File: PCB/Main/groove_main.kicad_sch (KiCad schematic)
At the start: 38 parts, among them J1 Left_X, J2 Left_Y, J3 Right_X, J4 Right_Y, J5 Left_X, J6 Left_Y, J7 Right_X, J8 Right_Y, U2 Pico, U3 CD4052B

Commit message: Main PCB progress 50%
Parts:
- removed D20, D21, D22, D23, D24: WS2812B_Unified, groove_pico:WS2812B-2835, symbol groove_pico:WS2812B_Unified
- added C1, C2, C3, C4, C5, C6, C7, C8, C9: 0.1uF, Capacitor_SMD:C_0603_1608Metric_Pad1.08x0.95mm_HandSolder, symbol Device:C
- added J10: Left_Y, groove_pico:Solder_3P_S, symbol Connector_Generic:Conn_01x03
- added J11: Right_X, groove_pico:Solder_3P_S, symbol Connector_Generic:Conn_01x03
- added J12: Right_Y, groove_pico:Solder_3P_S, symbol Connector_Generic:Conn_01x03
- added J9: Left_X, groove_pico:Solder_3P_S, symbol Connector_Generic:Conn_01x03
- added SW1, SW2, SW3: SWITCH_SPST, groove_pico:EVQP1K05M, symbol agg:SWITCH_SPST
- added U3: LM4040DBZ-3, Package_TO_SOT_SMD:SOT-23, symbol Reference_Voltage:LM4040DBZ-3
- J1, J2, J3, J4: footprint Connector_PinHeader_1.27mm:PinHeader_1x03_P1.27mm_Vertical -> groove_pico:SH1.25_Thruhole_3P
- J5, J6, J7, J8: footprint Connector_JST:JST_GH_BM03B-GHS-TBT_1x03-1MP_P1.25mm_Vertical -> groove_pico:SH1.25mm_3P_SMD
- renumbered U2 to U1, U3 to U2
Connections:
- net +3.3VADC: now also J1.3 (Pin_3), J2.3 (Pin_3), J3.3 (Pin_3), J4.3 (Pin_3), J5.3 (Pin_3), J6.3 (Pin_3), J7.3 (Pin_3), J8.3 (Pin_3), C9.1, J10.3 (Pin_3), J11.3 (Pin_3), J12.3 (Pin_3), J9.3 (Pin_3), U3.1 (K); no longer J1.1 (Pin_1), J2.1 (Pin_1), J3.1 (Pin_1), J4.1 (Pin_1), J5.1 (Pin_1), J6.1 (Pin_1), J7.1 (Pin_1), J8.1 (Pin_1)
- net +3V3: now also C3.1
- net +5V: now also C1.1, C2.1, C4.1, C5.1, C6.1, C7.1, C8.1
- net GND: now also C1.2, C2.2, C3.2, C4.2, C5.2, C6.2, C7.2, C8.2; no longer J1.3 (Pin_3), J2.3 (Pin_3), J3.3 (Pin_3), J4.3 (Pin_3), J5.3 (Pin_3), J6.3 (Pin_3), J7.3 (Pin_3), J8.3 (Pin_3)
- net LX: now also J9.2 (Pin_2)
- net LY: now also J10.2 (Pin_2)
- net RX: now also J11.2 (Pin_2)
- net RY: now also J12.2 (Pin_2)
- net GNDREF: now reaches U1.34 (GPIO28_ADC2)
- net GNDREF: now also J1.1 (Pin_1), J2.1 (Pin_1), J3.1 (Pin_1), J4.1 (Pin_1), J5.1 (Pin_1), J6.1 (Pin_1), J7.1 (Pin_1), J8.1 (Pin_1), C9.2, J10.1 (Pin_1), J11.1 (Pin_1), J12.1 (Pin_1), J9.1 (Pin_1), U3.2 (A)
- no-connect marks 33 -> 32

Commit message: Main PCB progress 70%
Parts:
- added D20, D21, D22, D23, D24, D25, D26, D27, D32, D33, D34, D35, D36, D37, D38, D39: WS2812B_Unified, groove_pico:WS2812B-4020, symbol groove_pico:WS2812B_Unified
- added D28, D29, D30, D31, D40, D41, D42, D43: WS2812B_Unified, groove_pico:WS2812B-4020_UP, symbol groove_pico:WS2812B_Unified
- added J13, J14: SW, groove_pico:Solder_1P, symbol Connector:TestPoint
- added J15, J19: V, groove_pico:Solder_1P, symbol Connector:TestPoint
- added J16, J20: LED, groove_pico:Solder_1P, symbol Connector:TestPoint
- added J18, J22: G, groove_pico:Solder_1P, symbol Connector:TestPoint
- added R4, R5: 10, Resistor_SMD:R_0603_1608Metric, symbol Device:R_Small
- added SCR1, SCR2, SCR3, SCR4, SCR5, SCR6, SCR7, SCR8: ScrewHole, groove_pico:Hole2.0, symbol groove_pico:ScrewHole
- added SW4, SW5: SWITCH_SPST, groove_pico:SW_Kailh_Choc_V1V2_1.00u_LED, symbol agg:SWITCH_SPST
- renumbered R2 to R1, R3 to R2, R1 to R3
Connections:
- net +5V: now also D20.V (VDD), D21.V (VDD), D22.V (VDD), D23.V (VDD), D24.V (VDD), D25.V (VDD), D26.V (VDD), D27.V (VDD), D28.V (VDD), D29.V (VDD), D30.V (VDD), D31.V (VDD), D32.V (VDD), D33.V (VDD), D34.V (VDD), D35.V (VDD), D36.V (VDD), D37.V (VDD), D38.V (VDD), D39.V (VDD), D40.V (VDD), D41.V (VDD), D42.V (VDD), D43.V (VDD), J15.1, J19.1
- net GND: now also SW1.2 ("~{"}), SW2.2 ("~{"}), SW3.2 ("~{"}), U1.13 (GND), U1.23 (GND), D20.G (VSS), D21.G (VSS), D22.G (VSS), D23.G (VSS), D24.G (VSS), D25.G (VSS), D26.G (VSS), D27.G (VSS), D28.G (VSS), D29.G (VSS), D30.G (VSS), D31.G (VSS), D32.G (VSS), D33.G (VSS), D34.G (VSS), D35.G (VSS), D36.G (VSS), D37.G (VSS), D38.G (VSS), D39.G (VSS), D40.G (VSS), D41.G (VSS), D42.G (VSS), D43.G (VSS), J18.1, J22.1, SW4.2 ("~{"}), SW5.2 ("~{"})
- net GNDREF: now also U1.33 (AGND); no longer U1.34 (GPIO28_ADC2)
- net RGB: now also U1.17 (GPIO13); no longer U1.16 (GPIO12)
- net at SW1.1 ("~{"}): now also U1.1 (GPIO0)
- net at U1.15 (GPIO11): now also R5.2
- net at U1.2 (GPIO1): now also SW2.1 ("~{"})
- net at U1.4 (GPIO2): now also SW3.1 ("~{"})
- new net: D20.I (In), J16.1, R4.1
- new net: D27.O (Out), D28.I (In)
- new net: D28.O (Out), D29.I (In)
- new net: D32.I (In), J20.1, R5.1
- new net: J13.1, SW4.1 ("~{"})
- new net: D35.O (Out), D36.I (In)
- new net: D36.O (Out), D37.I (In)
- new net: D29.O (Out), D30.I (In)
- new net: D30.O (Out), D31.I (In)
- new net: D41.O (Out), D42.I (In)
- new net: D42.O (Out), D43.I (In)
- new net: D34.O (Out), D35.I (In)
- new net: D20.O (Out), D21.I (In)
- new net: D21.O (Out), D22.I (In)
- new net: D22.O (Out), D23.I (In)
- new net: D23.O (Out), D24.I (In)
- new net: D26.O (Out), D27.I (In)
- new net: D33.O (Out), D34.I (In)
- new net: D37.O (Out), D38.I (In)
- new net: R4.2, U1.16 (GPIO12)
- new net: D38.O (Out), D39.I (In)
- new net: D39.O (Out), D40.I (In)
- new net: D25.O (Out), D26.I (In)
- new net: D40.O (Out), D41.I (In)
- new net: D32.O (Out), D33.I (In)
- new net: D24.O (Out), D25.I (In)
- new net: J14.1, SW5.1 ("~{"})
- no-connect marks 32 -> 26
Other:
- moved on the sheet: C1, C2, C3, C4, C5, C6, C7, C8, C9, R3

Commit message: Main PCB progress 85%
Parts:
- added J17, J21: LED, groove_pico:Solder_1P_S, symbol Connector:TestPoint
- added J23, J24: SW, groove_pico:Solder_1P_S, symbol Connector:TestPoint
- added J25, J26: V, groove_pico:Solder_1P_S, symbol Connector:TestPoint
- added J27, J28: G, groove_pico:Solder_1P_S, symbol Connector:TestPoint
- J13, J14, J15, J16, J18, J19, J20, J22: footprint groove_pico:Solder_1P -> groove_pico:Solder_1P_S
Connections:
- net +5V: now also J25.1, J26.1
- net GND: now also SW4.1 ("~{"}), SW5.1 ("~{"}), U1.8 (GND), U2.6 (INH), J27.1, J28.1; no longer SW4.2 ("~{"}), SW5.2 ("~{"}), U1.13 (GND)
- net at D20.I (In), J16.1: no longer R4.1
- net at D32.I (In), J20.1: no longer R5.1
- net at J13.1: now also SW4.2 ("~{"}); no longer SW4.1 ("~{"})
- net at U1.1 (GPIO0): now also SW3.1 ("~{"}); no longer SW1.1 ("~{"})
- net at U1.11 (GPIO8): now also J23.1
- net at U1.12 (GPIO9): now also J24.1
- net at U1.4 (GPIO2): now also SW1.1 ("~{"}); no longer SW3.1 ("~{"})
- net at U1.40 (VBUS): now also USB1.11 (VBUS), USB1.2 (VBUS)
- net at J14.1: now also SW5.2 ("~{"}); no longer SW5.1 ("~{"})
- net RGB: no longer names the net of R3.2, U1.17 (GPIO13)
- new net: J17.1, R4.1
- new net: J21.1, R5.1
- no-connect marks 26 -> 24
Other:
- moved on the sheet: J16, J20, R3, SW2

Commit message: Main PCB v1.0
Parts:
- added SCR10, SCR11, SCR12, SCR13, SCR14, SCR15, SCR16, SCR9: ScrewHole, groove_pico:Hole2.0, symbol groove_pico:ScrewHole
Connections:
- net GND: now also U1.28 (GND)
- net at J17.1, R4.1: now also D20.I (In), J16.1
- net at D32.I (In), J20.1: now also J21.1, R5.1
- net SW_L: now reaches J13.1, SW4.2 ("~{"})
- net SW_L: now also J24.1, U1.12 (GPIO9)
- net SW_R: now reaches J23.1, U1.11 (GPIO8)
- net SW_R: now also J14.1, SW5.2 ("~{"})
- no-connect marks 24 -> 25
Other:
- moved on the sheet: J21, R5

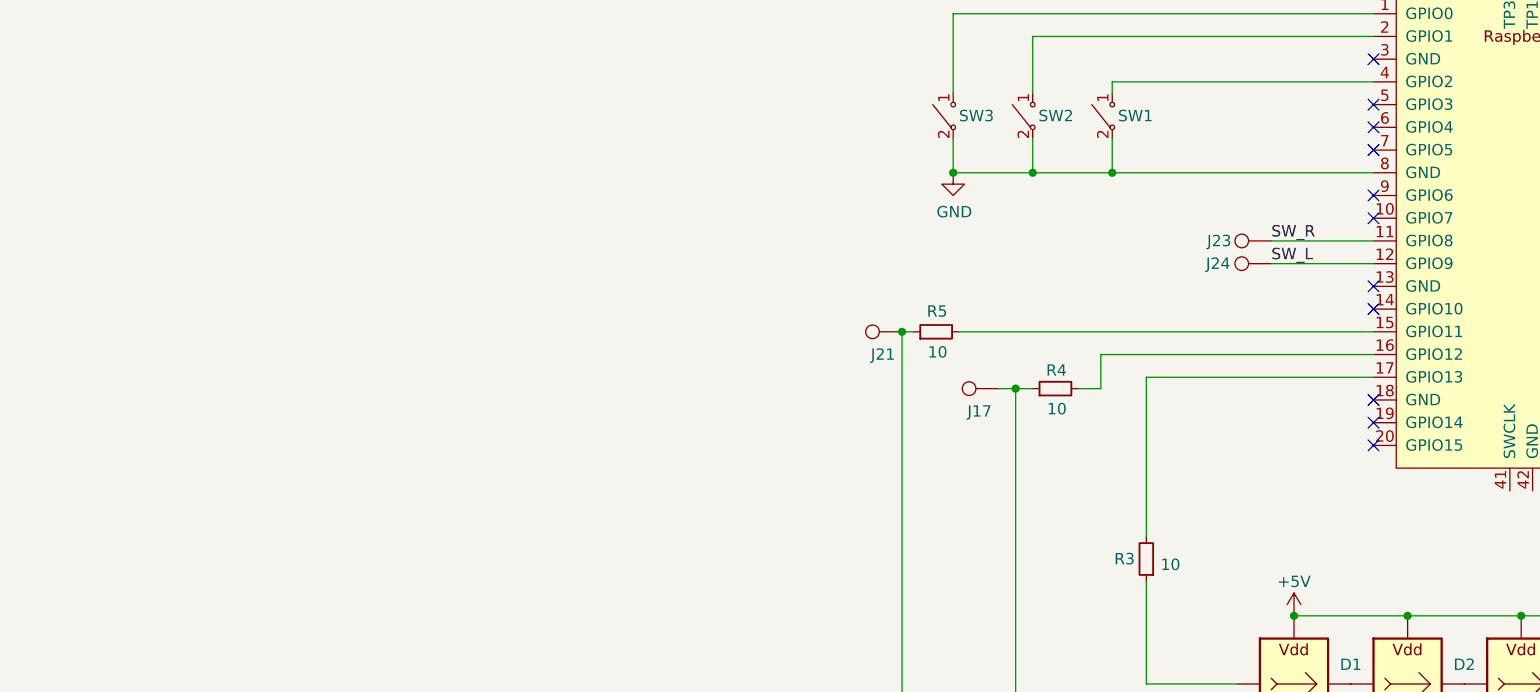
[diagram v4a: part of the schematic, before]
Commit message: Add slots in PCB for Hall gimbals
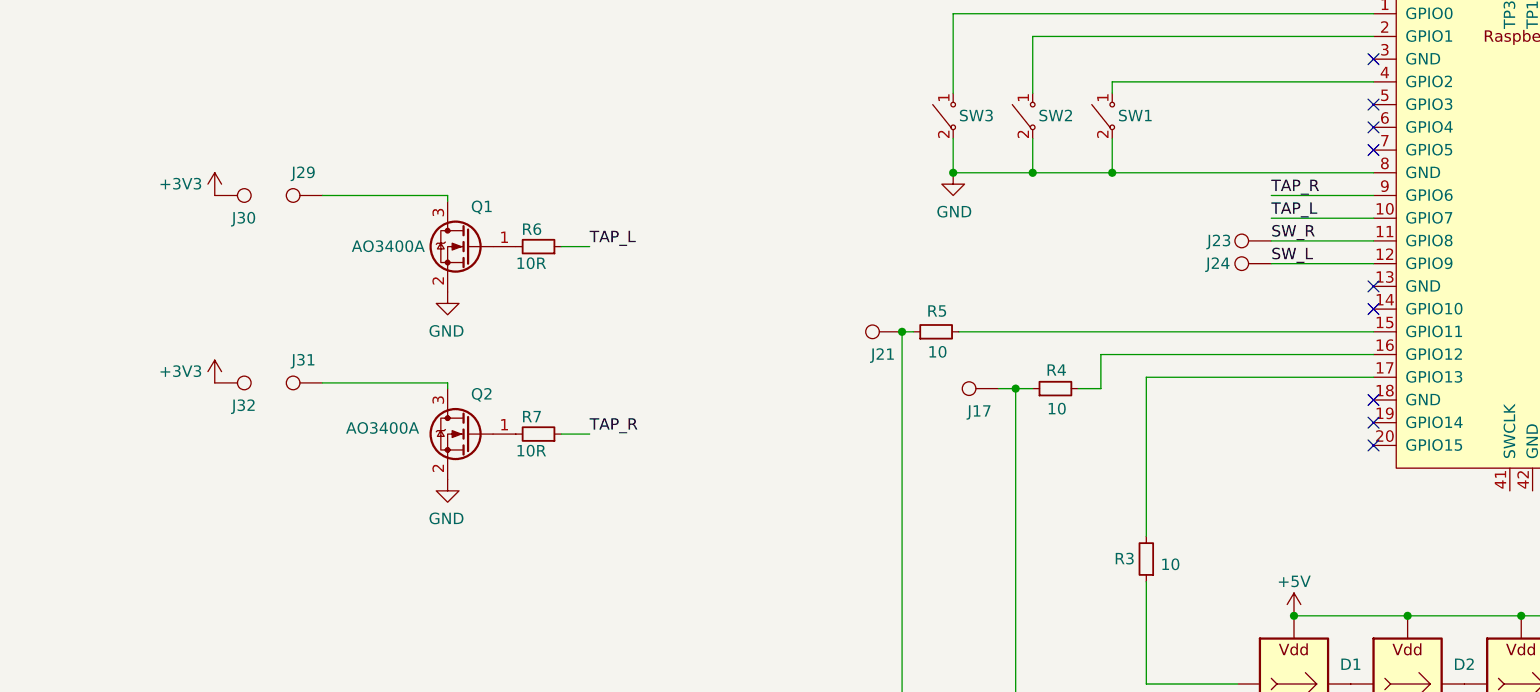
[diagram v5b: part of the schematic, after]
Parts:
- added J29, J31: HAP, groove_pico:Solder_1P_S, symbol Connector:TestPoint
- added J30, J32: V, groove_pico:Solder_1P_S, symbol Connector:TestPoint
- added Q1, Q2: AO3400A, Package_TO_SOT_SMD:SOT-23, symbol Transistor_FET:AO3400A
- added R6, R7: 10R, Resistor_SMD:R_0603_1608Metric, symbol Device:R_Small
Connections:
- net +3V3: now also J30.1, J32.1
- net GND: now also Q1.2 (S), Q2.2 (S)
- net TAP_L: now reaches U1.10 (GPIO7)
- net TAP_L: now also R6.1
- net TAP_R: now reaches U1.9 (GPIO6)
- net TAP_R: now also R7.1
- new net: Q2.1 (G), R7.2
- new net: J31.1, Q2.3 (D)
- new net: J29.1, Q1.3 (D)
- new net: Q1.1 (G), R6.2
- no-connect marks 25 -> 23

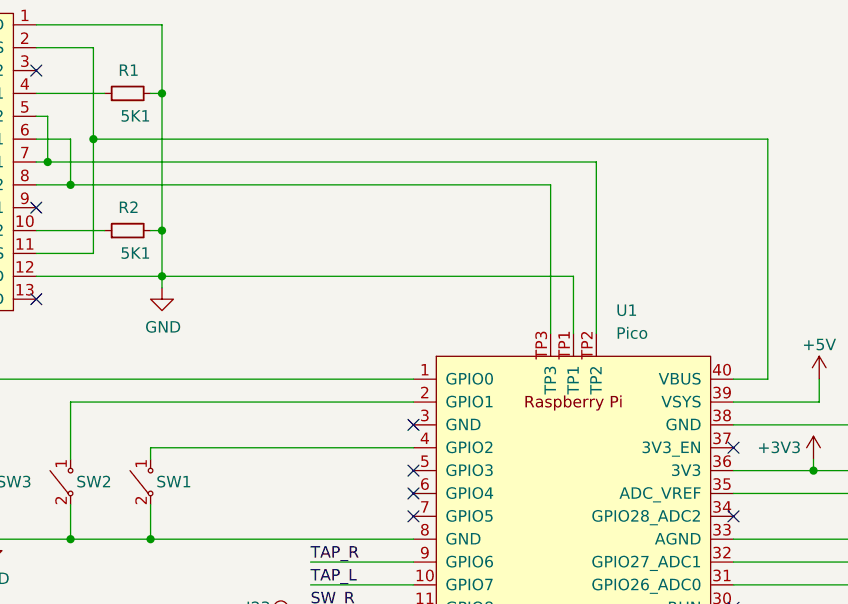
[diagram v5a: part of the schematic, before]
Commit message: PCB v1.2 (easier USB soldering holes)
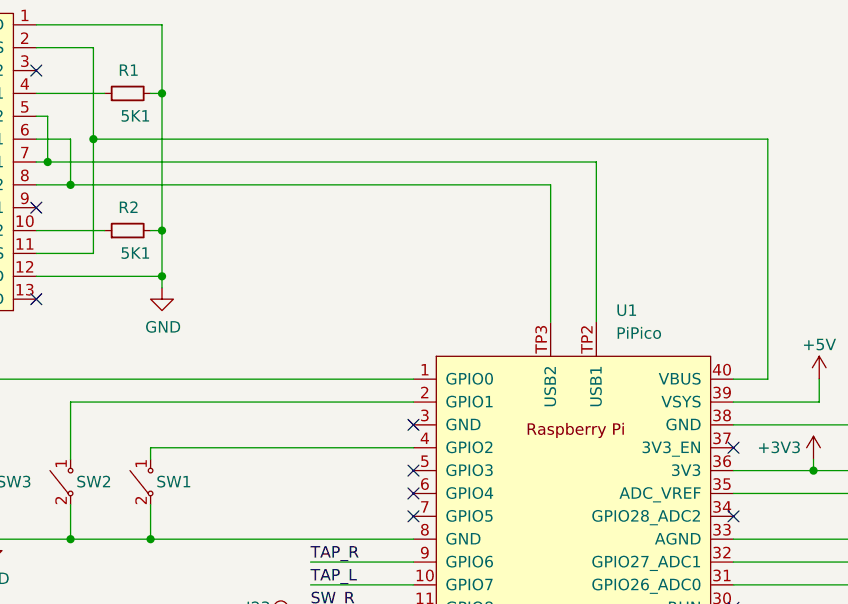
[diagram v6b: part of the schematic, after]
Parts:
- removed U1: Pico, groove_pico:RPi_Pico_SMD_Pins, symbol RP_Silicon_KiCad:Pico
- added U1: PiPico, groove_pico:RPi_Pico_SMD_Pins, symbol groove_pico:PiPico
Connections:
- net +3.3VADC: now also U1.35 (ADC_VREF)
- net +3V3: now also U1.36 (3V3)
- net +5V: now also U1.39 (VSYS)
- net GND: now also U1.23 (GND), U1.28 (GND), U1.38 (GND), U1.8 (GND)
- net GNDREF: now also U1.33 (AGND)
- net SW_L: now also U1.12 (GPIO9)
- net SW_R: now also U1.11 (GPIO8)
- net TAP_L: now also U1.10 (GPIO7)
- net TAP_R: now also U1.9 (GPIO6)
- net at R4.2: now also U1.16 (GPIO12)
- net at R3.2: now also U1.17 (GPIO13)
- net at SW3.1 ("~{"}): now also U1.1 (GPIO0)
- net at R5.2: now also U1.15 (GPIO11)
- net at SW2.1 ("~{"}): now also U1.2 (GPIO1)
- net at U2.9 (B): now also U1.26 (GPIO20)
- net at U2.10 (A): now also U1.27 (GPIO21)
- net at U2.3 (Y): now also U1.31 (GPIO26_ADC0)
- net at U2.13 (X): now also U1.32 (GPIO27_ADC1)
- net at SW1.1 ("~{"}): now also U1.4 (GPIO2)
- net at USB1.11 (VBUS), USB1.2 (VBUS): now also U1.40 (VBUS)
- net at USB1.5 (DN2), USB1.7 (DN1): now also U1.TP2 (USB1)
- net at USB1.6 (DP1), USB1.8 (DP2): now also U1.TP3 (USB2)
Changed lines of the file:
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@@
 	(wire
 		(pts
-			(xy 189.23 71.12) (xy 189.23 54.61)
-		)
-		(stroke
-			(width 0)
-			(type default)
-		)
-	)
-	(wire
-		(pts
 			(xy 146.05 44.45) (xy 146.05 59.69)
 		)
@@
 	(wire
 		(pts
-			(xy 191.77 64.77) (xy 146.05 64.77)
-		)
-		(stroke
-			(width 0)
-			(type default)
-		)
-	)
-	(wire
-		(pts
 			(xy 266.7 228.6) (xy 279.4 228.6)
 		)
@@
 	(wire
 		(pts
+			(xy 194.31 52.07) (xy 194.31 69.85)
+		)
+		(stroke
+			(width 0)
+			(type default)
+		)
+	)
+	(wire
+		(pts
 			(xy 203.2 213.36) (xy 215.9 213.36)
 		)
@@
 	(wire
 		(pts
-			(xy 191.77 71.12) (xy 191.77 64.77)
-		)
-		(stroke
-			(width 0)
-			(type default)
-		)
-	)
-	(wire
-		(pts
 			(xy 162.56 99.06) (xy 173.99 99.06)
 		)
@@
 	(wire
 		(pts
-			(xy 194.31 71.12) (xy 194.31 52.07)
-		)
-		(stroke
-			(width 0)
-			(type default)
-		)
-	)
-	(wire
-		(pts
 			(xy 102.87 214.63) (xy 102.87 218.44)
 		)
@@
 	(wire
 		(pts
+			(xy 189.23 54.61) (xy 189.23 69.85)
+		)
+		(stroke
+			(width 0)
+			(type default)
+		)
+	)
+	(wire
+		(pts
 			(xy 146.05 205.74) (xy 146.05 201.295)
 		)
@@
 	)
 	(symbol
-		(lib_id "RP_Silicon_KiCad:Pico")
-		(at 191.77 100.33 0)
-		(unit 1)
-		(exclude_from_sim no)
-		(in_bom yes)
-		(on_board yes)
-		(dnp no)
-		(fields_autoplaced yes)
-		(property "Reference" "U1"
-			(at 196.5041 68.58 0)
-			(effects
-				(font
-					(size 1.27 1.27)
-				)
-				(justify left)
-			)
-		)
-		(property "Value" "Pico"
-			(at 196.5041 71.12 0)
-			(effects
-				(font
-					(size 1.27 1.27)
-				)
-				(justify left)
-			)
-		)
-		(property "Footprint" "groove_pico:RPi_Pico_SMD_Pins"
-			(at 191.77 100.33 90)
-			(effects
-				(font
-					(size 1.27 1.27)
-				)
-				(hide yes)
-			)
-		)
-		(property "Datasheet" ""
-			(at 191.77 100.33 0)
-			(effects
-				(font
-					(size 1.27 1.27)
-				)
-				(hide yes)
-			)
-		)
-		(property "Description" ""
-			(at 191.77 100.33 0)
-			(effects
-				(font
-					(size 1.27 1.27)
-				)
-				(hide yes)
-			)
-		)
-		(pin "1"
-		)
-		(pin "10"
-		)
-		(pin "11"
-		)
-		(pin "12"
-		)
-		(pin "13"
-		)
-		(pin "14"
-		)
-		(pin "15"
-		)
-		(pin "16"
-		)
-		(pin "17"
-		)
-		(pin "18"
-		)
-		(pin "19"
-		)
-		(pin "2"
-		)
-		(pin "20"
-		)
-		(pin "21"
-		)
-		(pin "22"
-		)
-		(pin "23"
-		)
-		(pin "24"
-		)
-		(pin "25"
-		)
-		(pin "26"
-		)
-		(pin "27"
-		)
-		(pin "28"
-		)
-		(pin "29"
-		)
-		(pin "3"
-		)
-		(pin "30"
-		)
-		(pin "31"
-		)
-		(pin "32"
-		)
-		(pin "33"
-		)
-		(pin "34"
-		)
-		(pin "35"
-		)
-		(pin "36"
-		)
-		(pin "37"
-		)
-		(pin "38"
-		)
-		(pin "39"
-		)
-		(pin "4"
-		)
-		(pin "40"
-		)
-		(pin "41"
-		)
-		(pin "42"
-		)
-		(pin "43"
-		)
-		(pin "5"
-		)
-		(pin "6"
-		)
-		(pin "7"
-		)
-		(pin "8"
-		)
-		(pin "9"
-		)
-		(pin "TP1"
-		)
-		(pin "TP2"
-		)
-		(pin "TP3"
-		)
-		(instances
-			(project "groove_main"
-				(path "/2e3f5573-c264-4a8b-a2f0-0e6473d39aad"
-					(reference "U1")
-					(unit 1)
-				)
-			)
-		)
-	)
-	(symbol
 		(lib_id "Connector_Generic:Conn_01x03")
 		(at 360.68 111.76 0)
@@
 					(unit 1)
 				)
+			)
+		)
+	)
+	(symbol
+		(lib_id "groove_pico:PiPico")
+		(at 191.77 100.33 0)
+		(unit 1)
+		(exclude_from_sim no)
+		(in_bom yes)
+		(on_board yes)
+		(dnp no)
+		(fields_autoplaced yes)
+		(property "Reference" "U1"
+			(at 196.5041 68.58 0)
+			(effects
+				(font
+					(size 1.27 1.27)
+				)
+				(justify left)
+			)
+		)
+		(property "Value" "PiPico"
+			(at 196.5041 71.12 0)
+			(effects
+				(font
+					(size 1.27 1.27)
+				)
+				(justify left)
+			)
+		)
+		(property "Footprint" "groove_pico:RPi_Pico_SMD_Pins"
+			(at 191.77 100.33 90)
+			(effects
+				(font
+					(size 1.27 1.27)
+				)
+				(hide yes)
+			)
+		)
+		(property "Datasheet" ""
+			(at 191.77 100.33 0)
+			(effects
+				(font
+					(size 1.27 1.27)
+				)
+				(hide yes)
+			)
+		)
+		(property "Description" ""
+			(at 191.77 100.33 0)
+			(effects
+				(font
+					(size 1.27 1.27)
+				)
+				(hide yes)
+			)
+		)
+		(pin "26"
+		)
+		(pin "4"
+		)
+		(pin "5"
+		)
+		(pin "1"
+		)
+		(pin "13"
+		)
+		(pin "21"
+		)
+		(pin "17"
+		)
+		(pin "24"
+		)
+		(pin "32"
+		)
+		(pin "34"
+		)
+		(pin "10"
+		)
+		(pin "3"
+		)
+		(pin "30"
+		)
+		(pin "38"
+		)
+		(pin "15"
+		)
+		(pin "6"
+		)
+		(pin "8"
+		)
+		(pin "9"
+		)
+		(pin "31"
+		)
+		(pin "14"
+		)
+		(pin "2"
+		)
+		(pin "33"
+		)
+		(pin "39"
+		)
+		(pin "22"
+		)
+		(pin "28"
+		)
+		(pin "36"
+		)
+		(pin "19"
+		)
+		(pin "40"
+		)
+		(pin "43"
+		)
+		(pin "25"
+		)
+		(pin "41"
+		)
+		(pin "12"
+		)
+		(pin "16"
+		)
+		(pin "35"
+		)
+		(pin "37"
+		)
+		(pin "7"
+		)
+		(pin "TP2"
+		)
+		(pin "TP3"
+		)
+		(pin "11"
+		)
+		(pin "18"
+		)
+		(pin "20"
+		)
+		(pin "23"
+		)
+		(pin "29"
+		)
+		(pin "27"
+		)
+		(pin "42"
+		)
+		(instances
+			(project ""
+				(path "/2e3f5573-c264-4a8b-a2f0-0e6473d39aad"
+					(reference "U1")
+					(unit 1)
+				)
